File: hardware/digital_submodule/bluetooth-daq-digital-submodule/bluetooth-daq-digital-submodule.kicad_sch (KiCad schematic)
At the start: 142 parts, among them J1 MCU I/F, J2 Digital Inputs, J3 Digital Outputs, J4 Communication I/F, J5 RS-485 I/F, U1 74HC595, U2 74HC595, U3 74HC165, U4 74HC165, U5 24LC1025, U6 SN75176AD, U7 CD4053B, U8 CD4053B

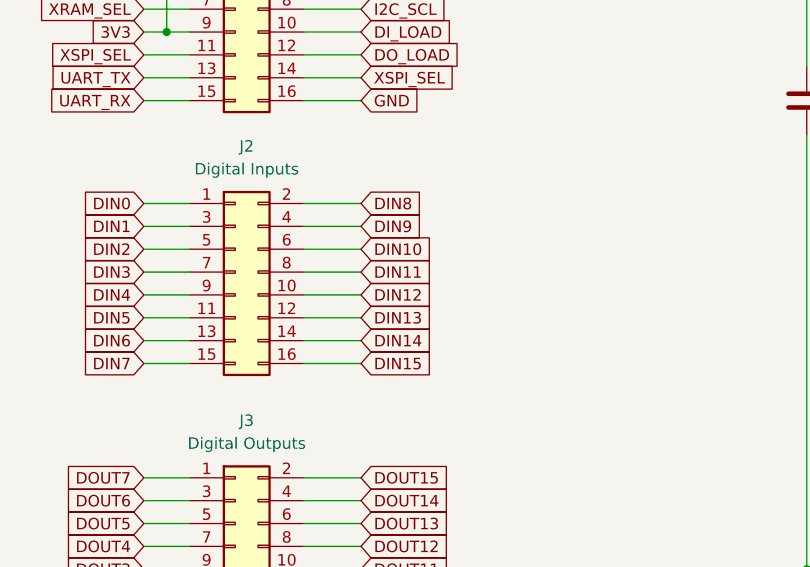
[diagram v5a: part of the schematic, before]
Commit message: Performed initial routing for digital submodule
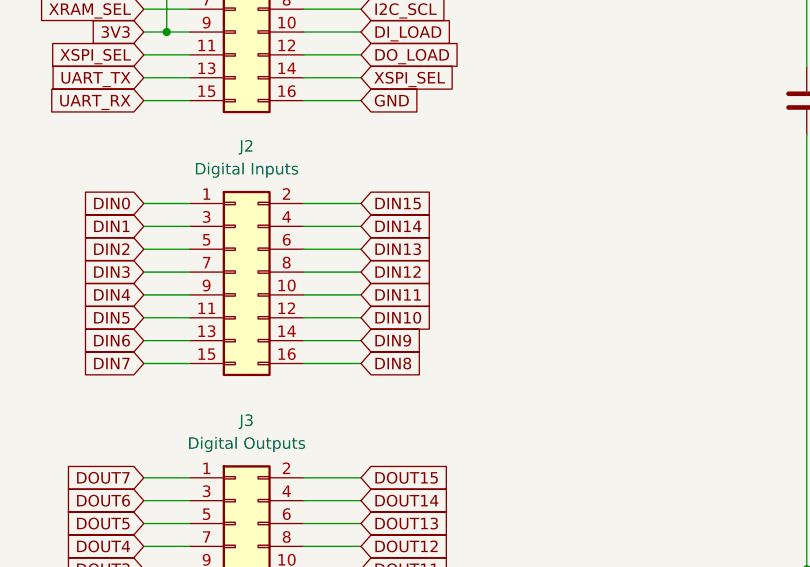
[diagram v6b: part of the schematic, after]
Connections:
- net DIN10: now also J2.12 (Pin_12); no longer J2.6 (Pin_6)
- net DIN11: now also J2.10 (Pin_10); no longer J2.8 (Pin_8)
- net DIN12: now also J2.8 (Pin_8); no longer J2.10 (Pin_10)
- net DIN13: now also J2.6 (Pin_6); no longer J2.12 (Pin_12)
- net DIN14: now also J2.4 (Pin_4); no longer J2.14 (Pin_14)
- net DIN15: now also J2.2 (Pin_2); no longer J2.16 (Pin_16)
- net DIN8: now also J2.16 (Pin_16); no longer J2.2 (Pin_2)
- net DIN9: now also J2.14 (Pin_14); no longer J2.4 (Pin_4)
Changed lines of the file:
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@@
     )
   )
-  (global_label "DIN9" (shape input) (at 60.96 68.58 0) (fields_autoplaced)
-    (effects (font (size 1.27 1.27)) (justify left))
-    (property "Intersheet References" "${INTERSHEET_REFS}" (id 0) (at 67.7879 68.5006 0)
+  (global_label "DIN14" (shape input) (at 60.96 68.58 0) (fields_autoplaced)
+    (effects (font (size 1.27 1.27)) (justify left))
+    (property "Intersheet References" "${INTERSHEET_REFS}" (id 0) (at 68.9974 68.5006 0)
       (effects (font (size 1.27 1.27)) (justify left) hide)
     )
@@
     )
   )
-  (global_label "DIN14" (shape input) (at 60.96 81.28 0) (fields_autoplaced)
-    (effects (font (size 1.27 1.27)) (justify left))
-    (property "Intersheet References" "${INTERSHEET_REFS}" (id 0) (at 68.9974 81.2006 0)
+  (global_label "DIN9" (shape input) (at 60.96 81.28 0) (fields_autoplaced)
+    (effects (font (size 1.27 1.27)) (justify left))
+    (property "Intersheet References" "${INTERSHEET_REFS}" (id 0) (at 67.7879 81.2006 0)
       (effects (font (size 1.27 1.27)) (justify left) hide)
     )
@@
     )
   )
-  (global_label "DIN13" (shape input) (at 60.96 78.74 0) (fields_autoplaced)
+  (global_label "DIN10" (shape input) (at 60.96 78.74 0) (fields_autoplaced)
     (effects (font (size 1.27 1.27)) (justify left))
     (property "Intersheet References" "${INTERSHEET_REFS}" (id 0) (at 68.9974 78.6606 0)
@@
     )
   )
-  (global_label "DIN10" (shape input) (at 60.96 71.12 0) (fields_autoplaced)
+  (global_label "DIN13" (shape input) (at 60.96 71.12 0) (fields_autoplaced)
     (effects (font (size 1.27 1.27)) (justify left))
     (property "Intersheet References" "${INTERSHEET_REFS}" (id 0) (at 68.9974 71.0406 0)
@@
     )
   )
-  (global_label "DIN8" (shape input) (at 60.96 66.04 0) (fields_autoplaced)
-    (effects (font (size 1.27 1.27)) (justify left))
-    (property "Intersheet References" "${INTERSHEET_REFS}" (id 0) (at 67.7879 65.9606 0)
+  (global_label "DIN15" (shape input) (at 60.96 66.04 0) (fields_autoplaced)
+    (effects (font (size 1.27 1.27)) (justify left))
+    (property "Intersheet References" "${INTERSHEET_REFS}" (id 0) (at 68.9974 65.9606 0)
       (effects (font (size 1.27 1.27)) (justify left) hide)
     )
@@
     )
   )
-  (global_label "DIN15" (shape input) (at 60.96 83.82 0) (fields_autoplaced)
-    (effects (font (size 1.27 1.27)) (justify left))
-    (property "Intersheet References" "${INTERSHEET_REFS}" (id 0) (at 68.9974 83.7406 0)
+  (global_label "DIN8" (shape input) (at 60.96 83.82 0) (fields_autoplaced)
+    (effects (font (size 1.27 1.27)) (justify left))
+    (property "Intersheet References" "${INTERSHEET_REFS}" (id 0) (at 67.7879 83.7406 0)
       (effects (font (size 1.27 1.27)) (justify left) hide)
     )
@@
     )
   )
-  (global_label "DIN11" (shape input) (at 60.96 73.66 0) (fields_autoplaced)
+  (global_label "DIN12" (shape input) (at 60.96 73.66 0) (fields_autoplaced)
     (effects (font (size 1.27 1.27)) (justify left))
     (property "Intersheet References" "${INTERSHEET_REFS}" (id 0) (at 68.9974 73.5806 0)
@@
     )
   )
-  (global_label "DIN12" (shape input) (at 60.96 76.2 0) (fields_autoplaced)
+  (global_label "DIN11" (shape input) (at 60.96 76.2 0) (fields_autoplaced)
     (effects (font (size 1.27 1.27)) (justify left))
     (property "Intersheet References" "${INTERSHEET_REFS}" (id 0) (at 68.9974 76.1206 0)

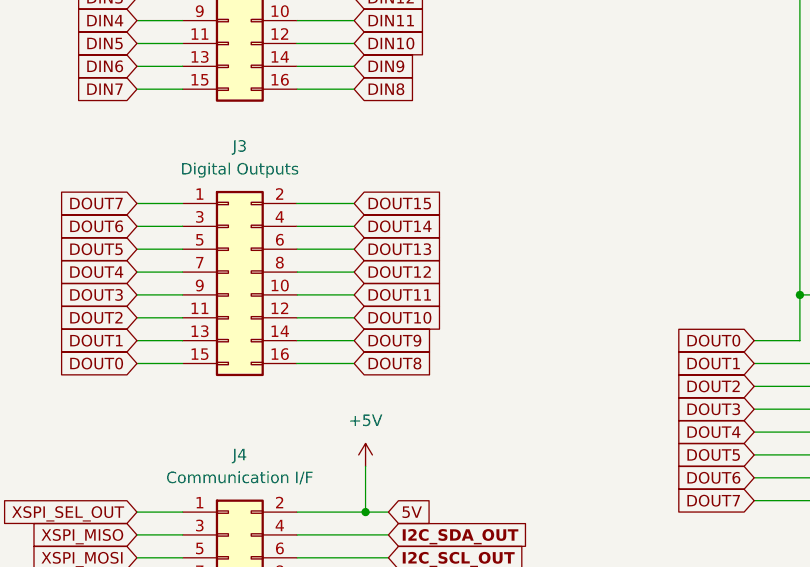
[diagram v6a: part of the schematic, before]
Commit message: Routed digital output 1 of digital submodule
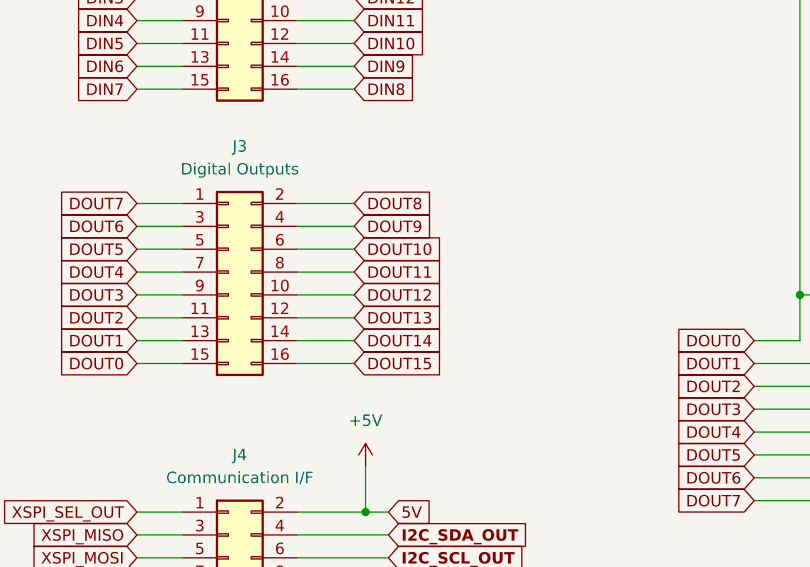
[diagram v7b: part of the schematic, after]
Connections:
- net DOUT10: now also J3.6 (Pin_6); no longer J3.12 (Pin_12)
- net DOUT11: now also J3.8 (Pin_8); no longer J3.10 (Pin_10)
- net DOUT12: now also J3.10 (Pin_10); no longer J3.8 (Pin_8)
- net DOUT13: now also J3.12 (Pin_12); no longer J3.6 (Pin_6)
- net DOUT14: now also J3.14 (Pin_14); no longer J3.4 (Pin_4)
- net DOUT15: now also J3.16 (Pin_16); no longer J3.2 (Pin_2)
- net DOUT8: now also J3.2 (Pin_2); no longer J3.16 (Pin_16)
- net DOUT9: now also J3.4 (Pin_4); no longer J3.14 (Pin_14)
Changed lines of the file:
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@@
     )
   )
-  (global_label "DOUT13" (shape input) (at 60.96 101.6 0) (fields_autoplaced)
+  (global_label "DOUT10" (shape input) (at 60.96 101.6 0) (fields_autoplaced)
     (effects (font (size 1.27 1.27)) (justify left))
     (property "Intersheet References" "${INTERSHEET_REFS}" (id 0) (at 70.6907 101.5206 0)
@@
     )
   )
-  (global_label "DOUT14" (shape input) (at 60.96 99.06 0) (fields_autoplaced)
-    (effects (font (size 1.27 1.27)) (justify left))
-    (property "Intersheet References" "${INTERSHEET_REFS}" (id 0) (at 70.6907 98.9806 0)
+  (global_label "DOUT9" (shape input) (at 60.96 99.06 0) (fields_autoplaced)
+    (effects (font (size 1.27 1.27)) (justify left))
+    (property "Intersheet References" "${INTERSHEET_REFS}" (id 0) (at 69.4812 98.9806 0)
       (effects (font (size 1.27 1.27)) (justify left) hide)
     )
@@
     )
   )
-  (global_label "DOUT12" (shape input) (at 60.96 104.14 0) (fields_autoplaced)
+  (global_label "DOUT11" (shape input) (at 60.96 104.14 0) (fields_autoplaced)
     (effects (font (size 1.27 1.27)) (justify left))
     (property "Intersheet References" "${INTERSHEET_REFS}" (id 0) (at 70.6907 104.0606 0)
@@
     )
   )
-  (global_label "DOUT9" (shape input) (at 60.96 111.76 0) (fields_autoplaced)
-    (effects (font (size 1.27 1.27)) (justify left))
-    (property "Intersheet References" "${INTERSHEET_REFS}" (id 0) (at 69.4812 111.6806 0)
+  (global_label "DOUT14" (shape input) (at 60.96 111.76 0) (fields_autoplaced)
+    (effects (font (size 1.27 1.27)) (justify left))
+    (property "Intersheet References" "${INTERSHEET_REFS}" (id 0) (at 70.6907 111.6806 0)
       (effects (font (size 1.27 1.27)) (justify left) hide)
     )
@@
     )
   )
-  (global_label "DOUT11" (shape input) (at 60.96 106.68 0) (fields_autoplaced)
+  (global_label "DOUT12" (shape input) (at 60.96 106.68 0) (fields_autoplaced)
     (effects (font (size 1.27 1.27)) (justify left))
     (property "Intersheet References" "${INTERSHEET_REFS}" (id 0) (at 70.6907 106.6006 0)
@@
     )
   )
-  (global_label "DOUT10" (shape input) (at 60.96 109.22 0) (fields_autoplaced)
+  (global_label "DOUT13" (shape input) (at 60.96 109.22 0) (fields_autoplaced)
     (effects (font (size 1.27 1.27)) (justify left))
     (property "Intersheet References" "${INTERSHEET_REFS}" (id 0) (at 70.6907 109.1406 0)
@@
     )
   )
-  (global_label "DOUT8" (shape input) (at 60.96 114.3 0) (fields_autoplaced)
-    (effects (font (size 1.27 1.27)) (justify left))
-    (property "Intersheet References" "${INTERSHEET_REFS}" (id 0) (at 69.4812 114.2206 0)
+  (global_label "DOUT15" (shape input) (at 60.96 114.3 0) (fields_autoplaced)
+    (effects (font (size 1.27 1.27)) (justify left))
+    (property "Intersheet References" "${INTERSHEET_REFS}" (id 0) (at 70.6907 114.2206 0)
       (effects (font (size 1.27 1.27)) (justify left) hide)
     )
@@
     )
   )
-  (global_label "DOUT15" (shape input) (at 60.96 96.52 0) (fields_autoplaced)
-    (effects (font (size 1.27 1.27)) (justify left))
-    (property "Intersheet References" "${INTERSHEET_REFS}" (id 0) (at 70.6907 96.4406 0)
-      (effects (font (size 1.27 1.27)) (justify left) hide)
-    )
+  (global_label "DOUT8" (shape input) (at 60.96 96.52 0) (fields_autoplaced)
+    (effects (font (size 1.27 1.27)) (justify left))
+    (property "Intersheet References" "${INTERSHEET_REFS}" (id 0) (at 69.4812 96.4406 0)
+      (effects (font (size 1.27 1.27)) (justify left) hide)
+    )

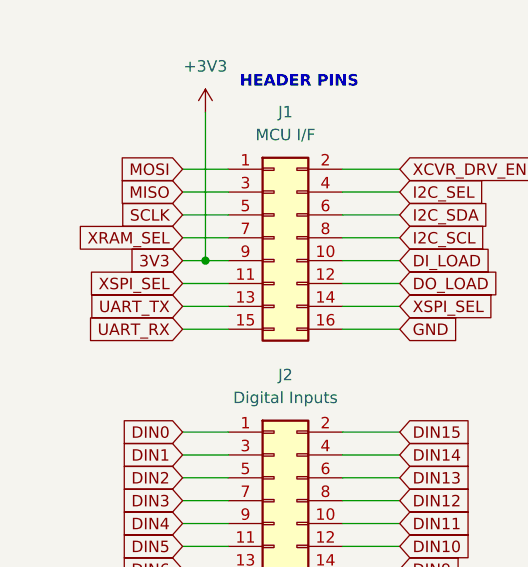
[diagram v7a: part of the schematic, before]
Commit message: Performed routing for interface section for digital submodule.
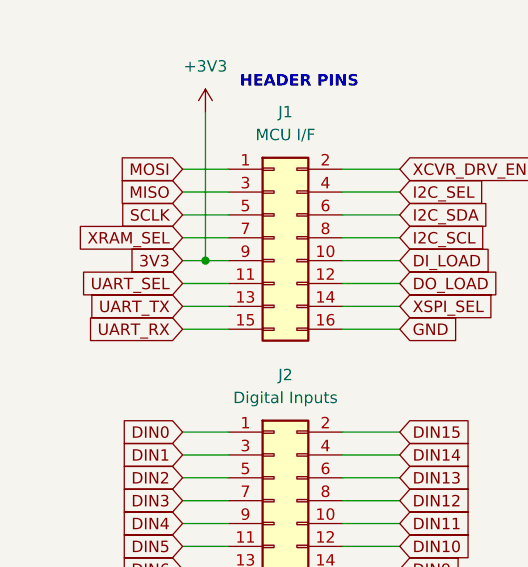
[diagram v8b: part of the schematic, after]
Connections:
- net UART_SEL: now also J1.11 (Pin_11)
- net XSPI_SEL: no longer J1.11 (Pin_11)
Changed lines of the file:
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@@
     )
   )
-  (global_label "XSPI_SEL" (shape input) (at 36.83 49.53 180) (fields_autoplaced)
+  (global_label "UART_SEL" (shape input) (at 36.83 49.53 180) (fields_autoplaced)
     (effects (font (size 1.27 1.27)) (justify right))
-    (property "Intersheet References" "${INTERSHEET_REFS}" (id 0) (at 25.7688 49.4506 0)
+    (property "Intersheet References" "${INTERSHEET_REFS}" (id 0) (at 25.4059 49.4506 0)
       (effects (font (size 1.27 1.27)) (justify right) hide)
     )
